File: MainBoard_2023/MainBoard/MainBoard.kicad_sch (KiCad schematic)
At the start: 53 parts, among them IC1 IP2721D, J1 UJC-HP-3-SMT-TR, J2 Conn_01x03, J3 Conn_01x02, J4 Micro_SD_Card_Det_Hirose_DM3AT, J5 Micro_SD_Card_Det_Hirose_DM3AT, Q1 AO3400A, SW1 RS_PRO_Slide_Switch, U1 Adafruit_BNO055_STEMMA_QT, U2 SEN0516, U3 Seeed_Studio_XIAO_nRF52840_Se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, U4 Pi Pico 0, U5 Pi Pico 1

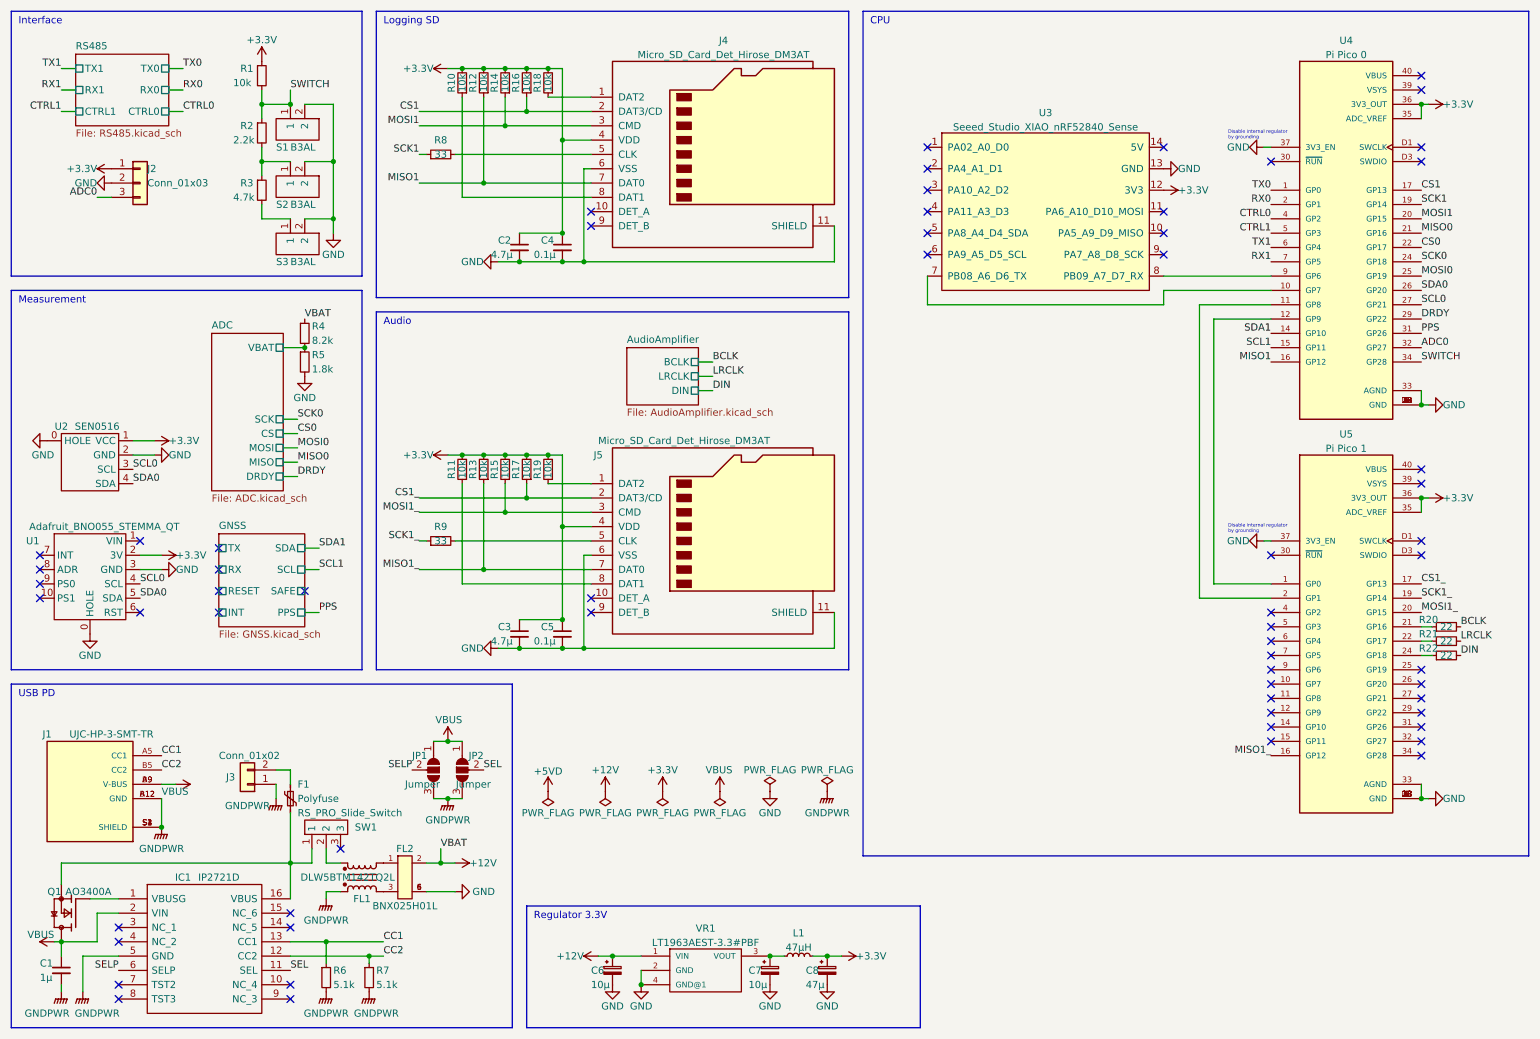
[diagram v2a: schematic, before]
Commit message: 回路図とPCBを変更
RJコネクタに変更
秋月のBNO055に変更
気圧センサのフットプリントを変更
ブロックタイプエミフィルのパッドを縮小
外形と取り付け穴を設定
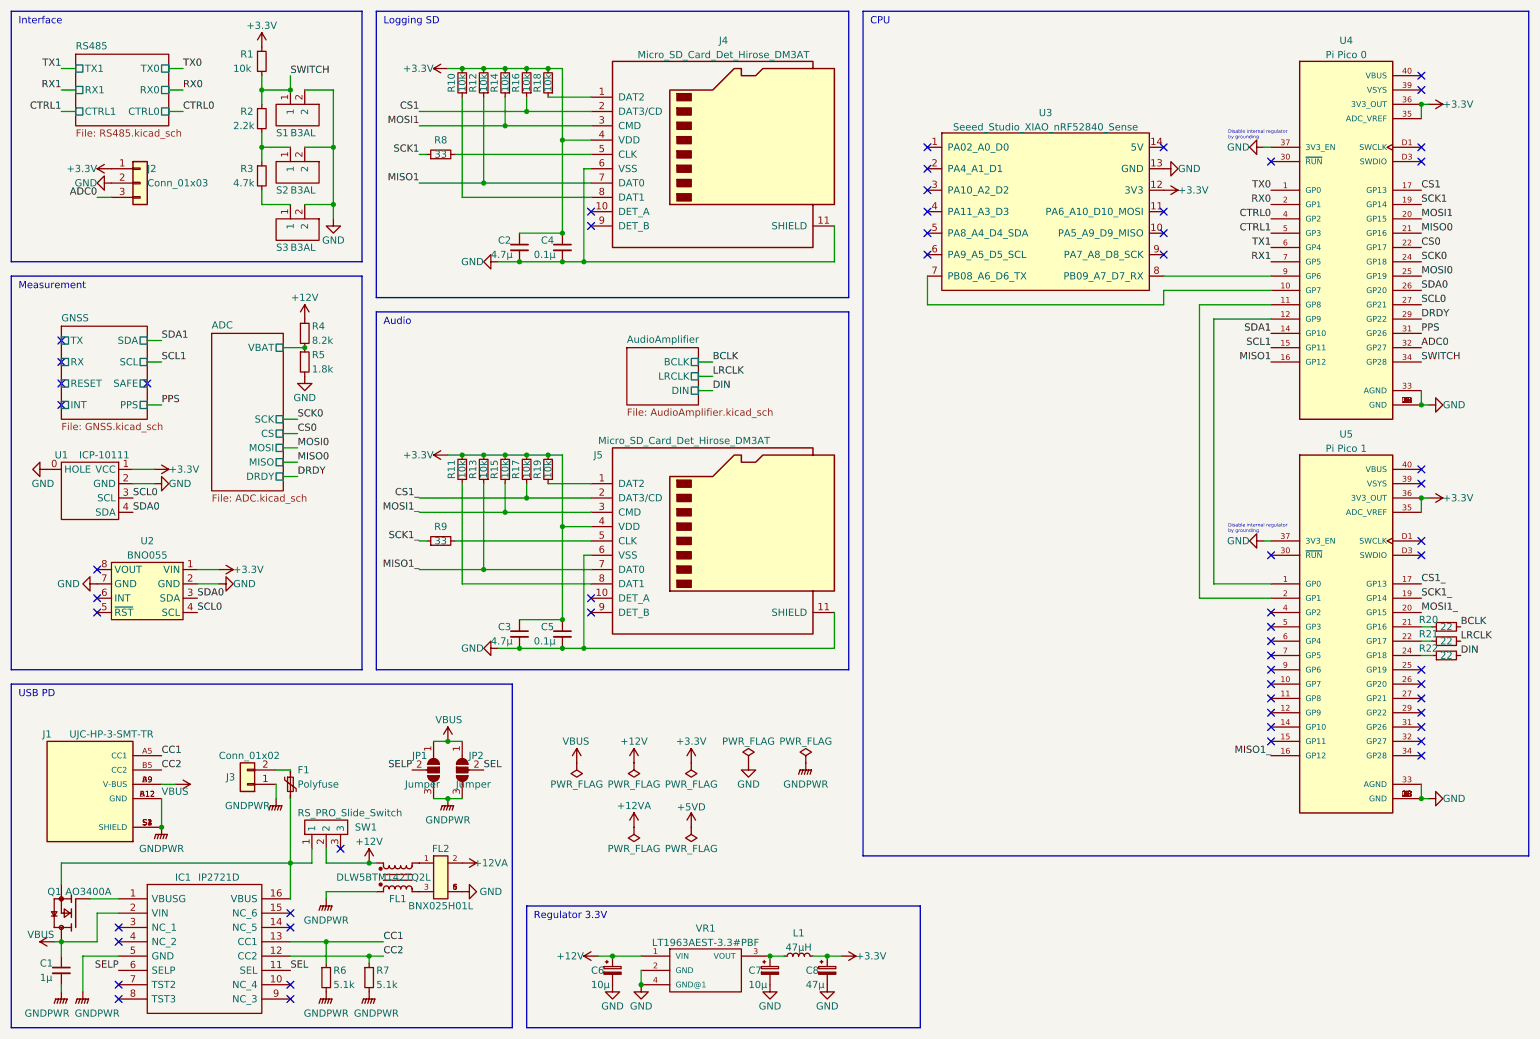
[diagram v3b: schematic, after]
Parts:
- removed U1: Adafruit_BNO055_STEMMA_QT, Adafruit_BNO055_STEMMA_QT:Adafruit_BNO055_STEMMA_QT, symbol Adafruit_BNO055_STEMMA_QT:Adafruit_BNO055_STEMMA_QT
- added U2: BNO055, Akizuki_BNO055:Akizuki_BNO055, symbol Akizuki_BNO055:Akizuki_BNO055
- U1: renamed from U2; value SEN0516 -> ICP-10111
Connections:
- net +12V: now also FL1.1, SW1.2; no longer FL2.2
- net +3.3V: now also U2.1 (VIN)
- net GND: now also U2.2 (GND), U2.7 (GND)
- net SCL0: now also U2.4 (SCL)
- net SDA0: now also U2.3 (SDA)
- new net +12VA: FL2.2
- no-connect marks 61 -> 58
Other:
- moved on the sheet: F1, FL1, FL2, R1, R2, R3, S1, S2, S3, U1

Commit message: シルクを整えた
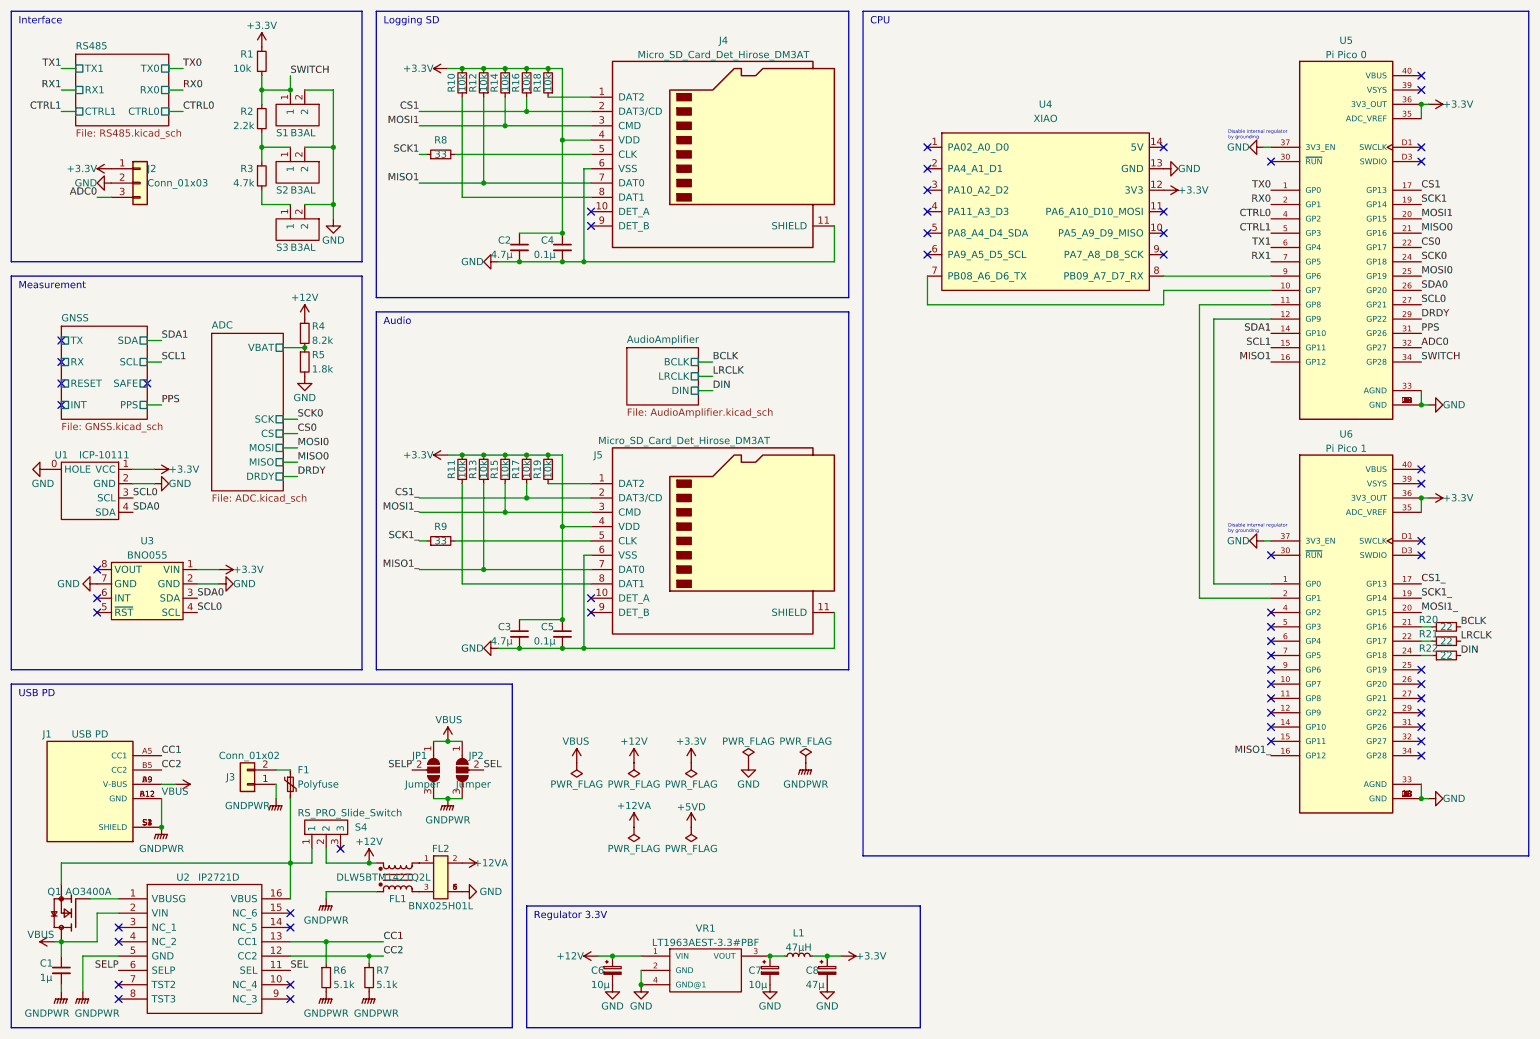
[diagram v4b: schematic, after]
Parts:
- J1: value UJC-HP-3-SMT-TR -> USB PD
- U4: renamed from U3; value Seeed_Studio_XIAO_nRF52840_Sense -> XIAO
- renumbered SW1 to S4, IC1 to U2, U2 to U3, U4 to U5, U5 to U6
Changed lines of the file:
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@@
   (symbol (lib_id "Raspberry_Pi_Pico:SC0915") (at 250.19 53.34 0) (unit 1)
     (in_bom yes) (on_board yes) (fields_autoplaced)
-    (property "Reference" "U4" (id 0) (at 250.825 19.1602 0))
+    (property "Reference" "U5" (id 0) (at 250.825 19.1602 0))
     (property "Value" "Pi Pico 0" (id 1) (at 250.825 21.6971 0))
     (property "Footprint" "Raspberry_Pi_Pico:Raspberry_Pi_Pico" (id 2) (at 238.76 66.04 0)
@@
   (symbol (lib_id "RS_PRO_PCB_Slide_Switch_SPDT_Latching_3A_120V_ac_Top:RS_PRO_PCB_Slide_Switch_SPDT_Latching_3A_120V_ac_Top") (at 69.85 158.75 0) (unit 1)
     (in_bom yes) (on_board yes)
-    (property "Reference" "SW1" (id 0) (at 74.93 158.75 0)
+    (property "Reference" "S4" (id 0) (at 74.93 158.75 0)
       (effects (font (size 1.27 1.27)) (justify left))
     )
@@
   (symbol (lib_id "Akizuki_BNO055:Akizuki_BNO055") (at 38.1 116.84 0) (mirror y) (unit 1)
     (in_bom yes) (on_board yes)
-    (property "Reference" "U2" (id 0) (at 38.1 107.95 0))
+    (property "Reference" "U3" (id 0) (at 38.1 107.95 0))
     (property "Value" "BNO055" (id 1) (at 38.1 110.49 0))
     (property "Footprint" "Akizuki_BNO055:Akizuki_BNO055" (id 2) (at 38.1 107.95 0)
@@
   (symbol (lib_id "Seeed_Studio_XIAO_nRF52840_Sense:Seeed_Studio_XIAO_nRF52840_Sense") (at 198.12 49.53 0) (unit 1)
     (in_bom yes) (on_board yes) (fields_autoplaced)
-    (property "Reference" "U3" (id 0) (at 197.485 31.9872 0))
-    (property "Value" "Seeed_Studio_XIAO_nRF52840_Sense" (id 1) (at 197.485 34.5241 0))
+    (property "Reference" "U4" (id 0) (at 197.485 30.48 0))
+    (property "Value" "XIAO" (id 1) (at 197.485 33.02 0))
     (property "Footprint" "Seeed_Studio_XIAO_nRF52840_Sense:Seeed_Studio_XIAO_nRF52840_Sense" (id 2) (at 189.23 44.45 0)
       (effects (font (size 1.27 1.27)) hide)
@@
   (symbol (lib_id "Raspberry_Pi_Pico:SC0915") (at 250.19 123.19 0) (unit 1)
     (in_bom yes) (on_board yes) (fields_autoplaced)
-    (property "Reference" "U5" (id 0) (at 250.825 89.0102 0))
+    (property "Reference" "U6" (id 0) (at 250.825 89.0102 0))
     (property "Value" "Pi Pico 1" (id 1) (at 250.825 91.5471 0))
     (property "Footprint" "Raspberry_Pi_Pico:Raspberry_Pi_Pico" (id 2) (at 238.76 135.89 0)
@@
   (symbol (lib_id "IP2721:IP2721D") (at 33.02 171.45 0) (unit 1)
     (in_bom yes) (on_board yes)
-    (property "Reference" "IC1" (id 0) (at 44.45 167.64 0))
+    (property "Reference" "U2" (id 0) (at 44.45 167.64 0))
     (property "Value" "IP2721D" (id 1) (at 50.8 167.64 0))
     (property "Footprint" "IP2721:IP2721" (id 2) (at 59.69 168.91 0)
@@
     (in_bom yes) (on_board yes)
     (property "Reference" "J1" (id 0) (at 20.32 142.24 0))
-    (property "Value" "UJC-HP-3-SMT-TR" (id 1) (at 31.75 142.24 0))
+    (property "Value" "USB PD" (id 1) (at 27.94 142.24 0))
     (property "Footprint" "USB_TypeC_6PIN:USB_TypeC_6PIN" (id 2) (at 27.94 151.13 0)
       (effects (font (size 1.27 1.27)) (justify left bottom) hide)
@@
     )
     (path "/f85cf890-aa32-4504-b508-c8edf9387b44/c65e2d05-742a-49dc-bab5-27309d0aeb2f"
-      (reference "ANT1") (unit 1) (value "SAM-M10Q-00B") (footprint "SAM-M10Q-00B:SAM-M10Q-00B")
+      (reference "ANT1") (unit 1) (value "SAM-M10Q") (footprint "SAM-M10Q-00B:SAM-M10Q-00B")
     )
     (path "/f85cf890-aa32-4504-b508-c8edf9387b44/beb2534f-787c-4f70-ad66-4383f30c6058"
-      (reference "BT1") (unit 1) (value "ML-1220_F1AN") (footprint "ML-1220_F1AN:ML-1220_F1AN")
+      (reference "BT1") (unit 1) (value "ML1220") (footprint "ML-1220_F1AN:ML-1220_F1AN")
     )
     (path "/a96dc772-4cb9-4e91-80d5-bc85b1486d9b"
@@
     )
     (path "/f85cf890-aa32-4504-b508-c8edf9387b44/fcb1fc09-ad18-4d40-9e72-50a0e0b0c642"
-      (reference "D2") (unit 1) (value "LED_Small") (footprint "LED_SMD:LED_1206_3216Metric_Pad1.42x1.75mm_HandSolder")
+      (reference "D2") (unit 1) (value "PPS") (footprint "LED_SMD:LED_1206_3216Metric_Pad1.42x1.75mm_HandSolder")
     )
     (path "/46543336-267d-43e5-b831-f6df35ec81a6"
@@
       (reference "FL2") (unit 1) (value "BNX025H01L") (footprint "BNX025H01:BNX025H01")
     )
-    (path "/7bc22fed-beb6-4e1a-8119-b4e39cb6d52a"
-      (reference "IC1") (unit 1) (value "IP2721D") (footprint "IP2721:IP2721")
-    )
-    (path "/a698e864-5ea2-4d35-b476-7712f47bb4e4/da6a917c-e84a-41a4-ba47-eb6bf0ce1682"
-      (reference "IC2") (unit 1) (value "ADS1120IPWR") (footprint "ADS1120IPWR:ADS1120IPWR")
-    )
     (path "/a2388978-fd17-4993-a4f9-c3a9179d6dfc"
-      (reference "J1") (unit 1) (value "UJC-HP-3-SMT-TR") (footprint "USB_TypeC_6PIN:USB_TypeC_6PIN")
+      (reference "J1") (unit 1) (value "USB PD") (footprint "USB_TypeC_6PIN:USB_TypeC_6PIN")
     )
     (path "/b4fd5145-d672-45b2-af6d-09d71c30c122"
@@
       (reference "S3") (unit 1) (value "B3AL") (footprint "B3AL-1002P-MS:B3AL-1002P-MS")
     )
+    (path "/2ba53bb7-1045-4441-bf07-c007c131b968"
+      (reference "S4") (unit 1) (value "RS_PRO_Slide_Switch") (footprint "RS_PRO_PCB_Slide_Switch_SPDT_Latching_3A_120V_ac_Top:RS_PRO_PCB_Slide_Switch_SPDT_Latching_3A_120V_ac_Top")
+    )
+    (path "/6a473b76-9def-47b1-bd12-ebbe49093892/a0abd0b9-06e2-4001-8134-c9815ffb8734"
+      (reference "S5") (unit 1) (value "A6S-7104-H") (footprint "A6S-7104-H:A6S-7104-H")
+    )
     (path "/8f1460a1-bf5a-4b04-9570-47768632e84c/fc0e0df3-49e3-4c23-be5b-abda2c8a8c68"
-      (reference "S4") (unit 1) (value "A6S3104H") (footprint "A6S-3104-H:A6S-3104-H")
-    )
-    (path "/2ba53bb7-1045-4441-bf07-c007c131b968"
-      (reference "SW1") (unit 1) (value "RS_PRO_Slide_Switch") (footprint "RS_PRO_PCB_Slide_Switch_SPDT_Latching_3A_120V_ac_Top:RS_PRO_PCB_Slide_Switch_SPDT_Latching_3A_120V_ac_Top")
-    )
-    (path "/6a473b76-9def-47b1-bd12-ebbe49093892/a0abd0b9-06e2-4001-8134-c9815ffb8734"
-      (reference "SW2") (unit 1) (value "A6S-7104-H") (footprint "A6S-7104-H:A6S-7104-H")
+      (reference "S6") (unit 1) (value "A6S3104H") (footprint "A6S-3104-H:A6S-3104-H")
     )
     (path "/5191b0dd-08a0-48e6-8519-2366babca68f"
       (reference "U1") (unit 1) (value "ICP-10111") (footprint "Fermion_Pressure_Sensor_ICP_10111:Fermion_Pressure_Sensor_ICP_10111")
     )
+    (path "/7bc22fed-beb6-4e1a-8119-b4e39cb6d52a"
+      (reference "U2") (unit 1) (value "IP2721D") (footprint "IP2721:IP2721")
+    )
     (path "/2e66279b-9e64-4d12-83bb-181f09223ebb"
-      (reference "U2") (unit 1) (value "BNO055") (footprint "Akizuki_BNO055:Akizuki_BNO055")
+      (reference "U3") (unit 1) (value "BNO055") (footprint "Akizuki_BNO055:Akizuki_BNO055")
     )
     (path "/3ff99bc4-fcbb-4818-8b05-ecfe050cac48"
-      (reference "U3") (unit 1) (value "Seeed_Studio_XIAO_nRF52840_Sense") (footprint "Seeed_Studio_XIAO_nRF52840_Sense:Seeed_Studio_XIAO_nRF52840_Sense")
+      (reference "U4") (unit 1) (value "XIAO") (footprint "Seeed_Studio_XIAO_nRF52840_Sense:Seeed_Studio_XIAO_nRF52840_Sense")
     )
     (path "/14be386e-a3c0-4598-8b97-aa4d0351a613"
-      (reference "U4") (unit 1) (value "Pi Pico 0") (footprint "Raspberry_Pi_Pico:Raspberry_Pi_Pico")
+      (reference "U5") (unit 1) (value "Pi Pico 0") (footprint "Raspberry_Pi_Pico:Raspberry_Pi_Pico")
     )
     (path "/48ed93ac-682a-4b2a-a871-860ff007f015"
-      (reference "U5") (unit 1) (value "Pi Pico 1") (footprint "Raspberry_Pi_Pico:Raspberry_Pi_Pico")
+      (reference "U6") (unit 1) (value "Pi Pico 1") (footprint "Raspberry_Pi_Pico:Raspberry_Pi_Pico")
     )
     (path "/6a473b76-9def-47b1-bd12-ebbe49093892/d4760016-19c4-42b8-a37d-f3df05c0496e"
-      (reference "U6") (unit 1) (value "YDA142") (footprint "YDA142:YDA142")
+      (reference "U7") (unit 1) (value "YDA142") (footprint "YDA142:YDA142")
     )
     (path "/8f1460a1-bf5a-4b04-9570-47768632e84c/cc972d28-908b-41a1-9f3b-d545f3aaeb40"
-      (reference "U7") (unit 1) (value "MAX3485") (footprint "MAX3485ECSA:MAX3485ECSA")
+      (reference "U8") (unit 1) (value "MAX3485") (footprint "MAX3485ECSA:MAX3485ECSA")
     )
     (path "/8f1460a1-bf5a-4b04-9570-47768632e84c/e5f0d2d2-0c1e-45b1-a504-85a89648e051"
-      (reference "U8") (unit 1) (value "TC7S14F") (footprint "TC7S14F:TC7S14F")
+      (reference "U9") (unit 1) (value "TC7S14F") (footprint "TC7S14F:TC7S14F")
     )
     (path "/8f1460a1-bf5a-4b04-9570-47768632e84c/bd02e4dd-3d59-4efc-9c1d-18d784fef2cc"
-      (reference "U9") (unit 1) (value "LTC1480CN8#PBF") (footprint "Package_DIP:DIP-8_W7.62mm_LongPads")
+      (reference "U10") (unit 1) (value "LTC1480CN8#PBF") (footprint "Package_DIP:DIP-8_W7.62mm_LongPads")
     )
     (path "/8f1460a1-bf5a-4b04-9570-47768632e84c/b65d99ac-99bd-4888-84d7-413f954a898f"
-      (reference "U10") (unit 1) (value "MAX3485") (footprint "MAX3485ECSA:MAX3485ECSA")
+      (reference "U11") (unit 1) (value "MAX3485") (footprint "MAX3485ECSA:MAX3485ECSA")
     )
     (path "/8f1460a1-bf5a-4b04-9570-47768632e84c/51c82790-8ed3-46aa-be36-22fd8517e36c"
-      (reference "U11") (unit 1) (value "LTC1480CN8#PBF") (footprint "Package_DIP:DIP-8_W7.62mm_LongPads")
+      (reference "U12") (unit 1) (value "LTC1480CN8#PBF") (footprint "Package_DIP:DIP-8_W7.62mm_LongPads")
     )
     (path "/8f1460a1-bf5a-4b04-9570-47768632e84c/a1122634-775a-46f3-987b-36d156968557"
-      (reference "U12") (unit 1) (value "MAX3485") (footprint "MAX3485ECSA:MAX3485ECSA")
+      (reference "U13") (unit 1) (value "MAX3485") (footprint "MAX3485ECSA:MAX3485ECSA")
     )
     (path "/8f1460a1-bf5a-4b04-9570-47768632e84c/3ef87d4c-73b2-4ae8-b991-7c23d306a0e6"
-      (reference "U13") (unit 1) (value "LTC1480CN8#PBF") (footprint "Package_DIP:DIP-8_W7.62mm_LongPads")
+      (reference "U14") (unit 1) (value "LTC1480CN8#PBF") (footprint "Package_DIP:DIP-8_W7.62mm_LongPads")
+    )
+    (path "/a698e864-5ea2-4d35-b476-7712f47bb4e4/da6a917c-e84a-41a4-ba47-eb6bf0ce1682"
+      (reference "U15") (unit 1) (value "ADS1120IPWR") (footprint "ADS1120IPWR:ADS1120IPWR")
     )
     (path "/5d211f61-54bd-4b78-a50b-2f1f8ec59693"
